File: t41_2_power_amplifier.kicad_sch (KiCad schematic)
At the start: 44 parts, among them J1 5-1814832-1, J2 5-1814832-1, J3 B2B-XH-A_LF__SN_, J5 Screw_Terminal_01x02, Q1 Q_NMOS_GSD, Q3 Q_NMOS_GSD, T1 Transformer_1P_SS, T2 Transformer_1P_1S, U1 MCP1802x-xx02xOT

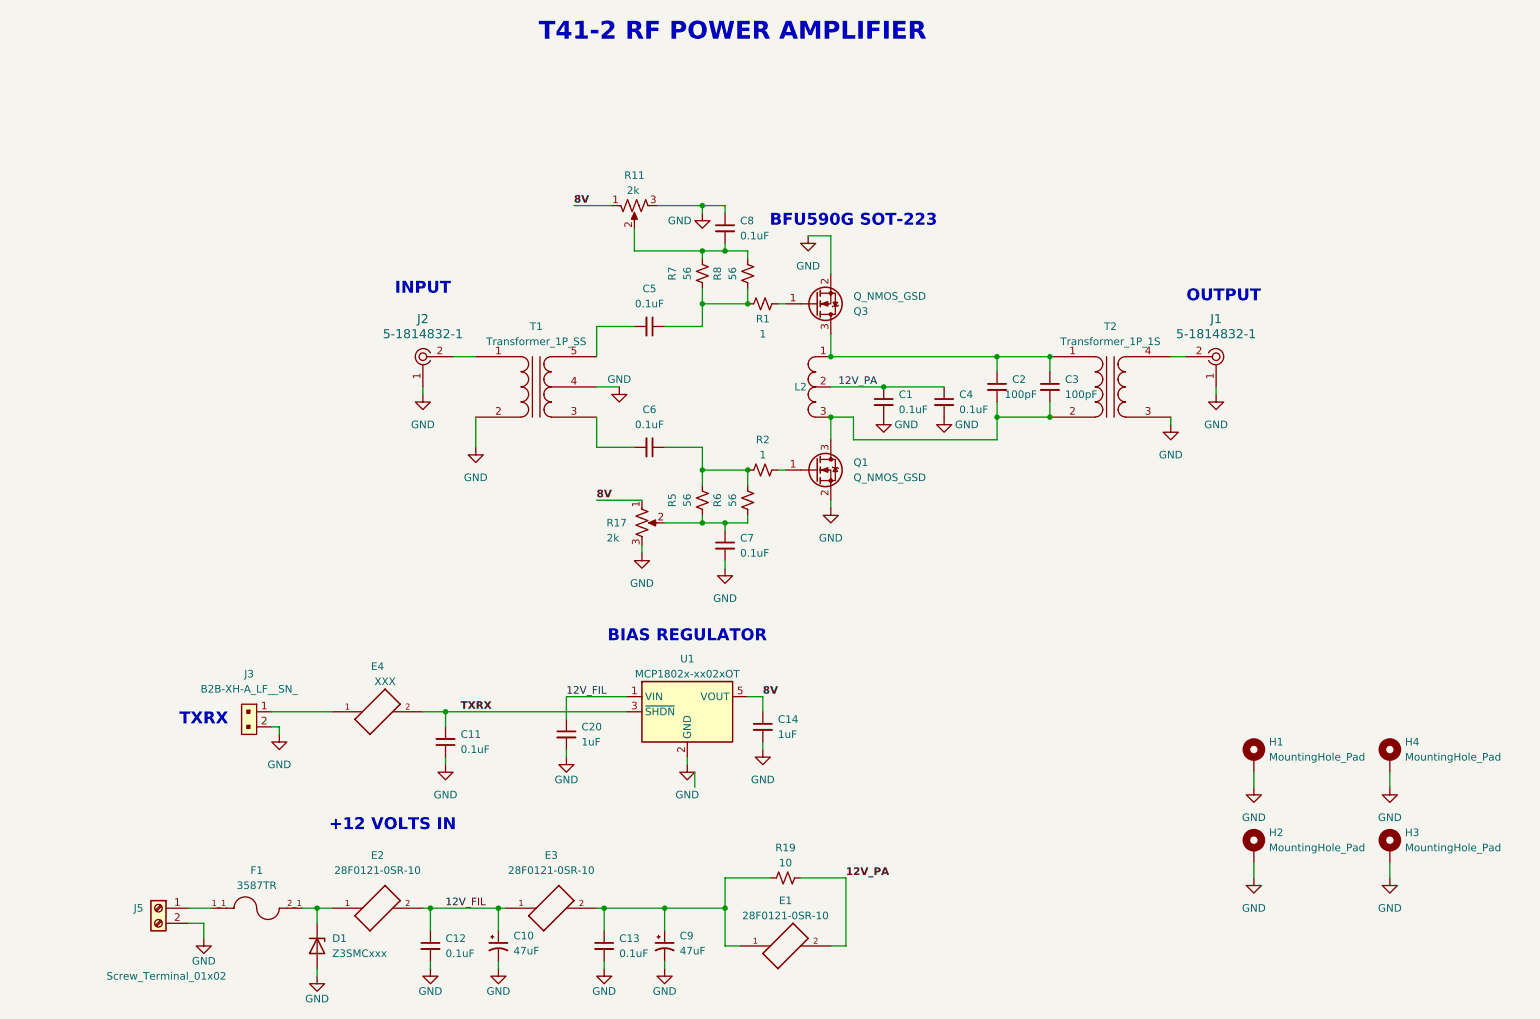
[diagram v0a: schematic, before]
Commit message: Larger output balun design to fab.
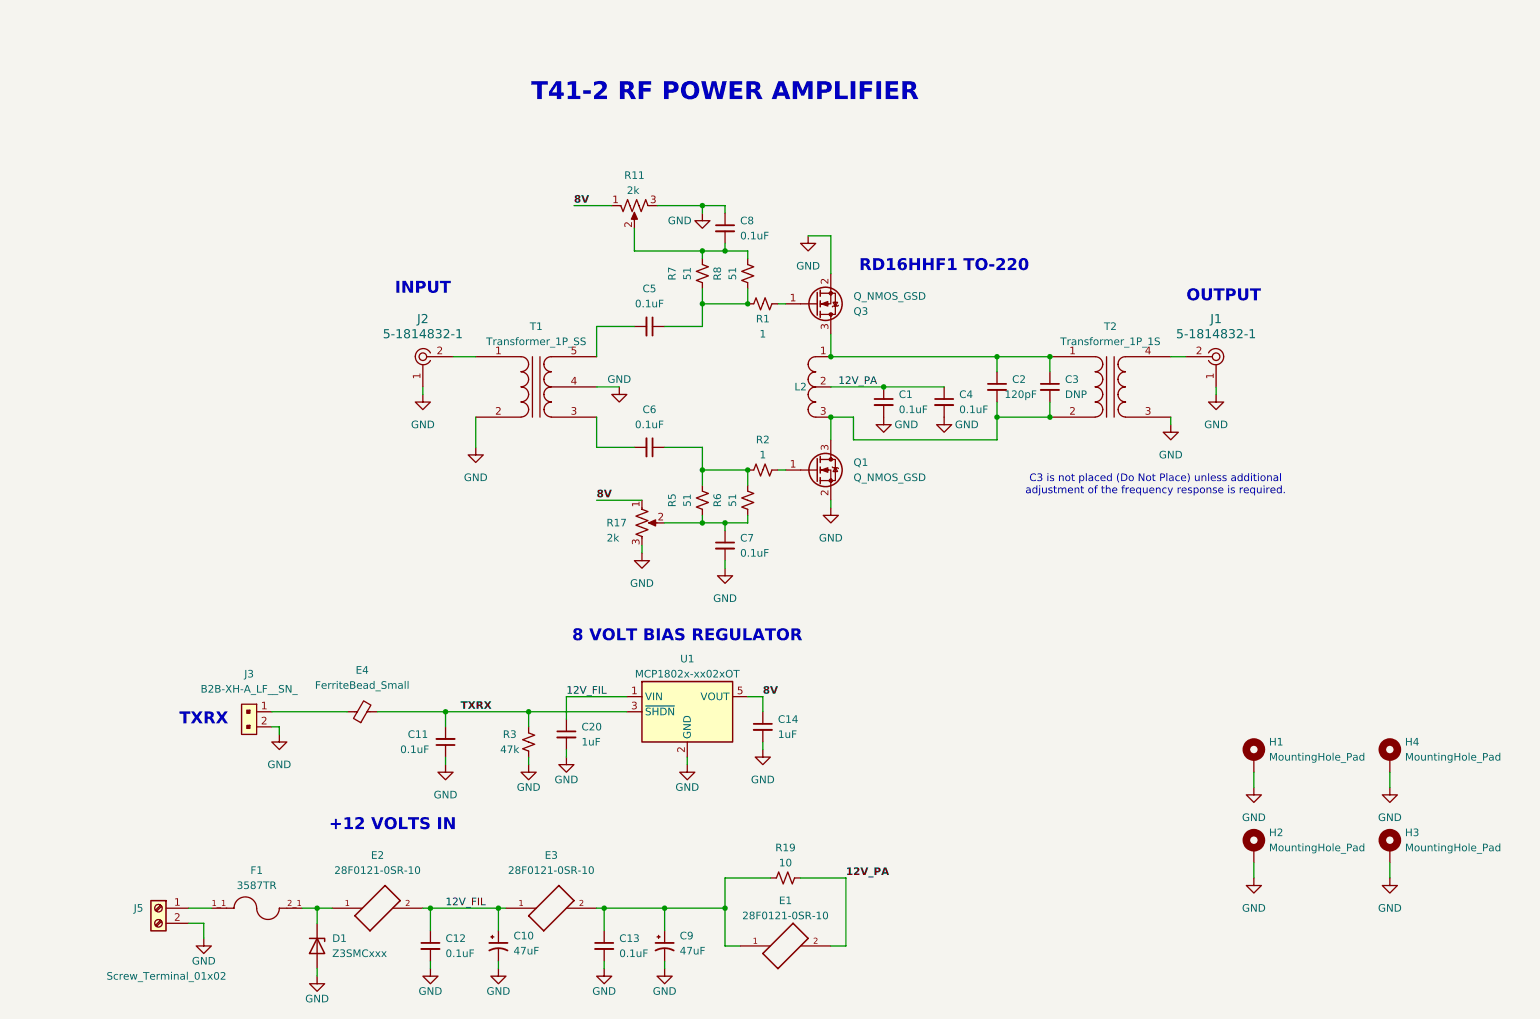
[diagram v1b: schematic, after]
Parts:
- removed E4: XXX, Inductor_SMD:L_1206_3216Metric, symbol 28F0121-0SR-10:28F0121-0SR-10
- added E4: FerriteBead_Small, Inductor_SMD:L_1206_3216Metric, symbol Device:FerriteBead_Small
- added R3: 47k, Resistor_SMD:R_1206_3216Metric, symbol Device:R_Small_US
- C2: value 100pF -> 120pF
- C3: value 100pF -> DNP
- R5, R6, R7, R8: value 56 -> 51
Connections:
- net GND: now also R3.1
- net TXRX: now also E4.2, R3.2
- net at J3.1: now also E4.1
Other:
- note added: "8 VOLT BIAS REGULATOR"
- note added: "C3 is not placed (Do Not Place) unless additional adjustment of the frequency response is required."
- note added: "RD16HHF1 TO-220"
- note removed: "BFU590G SOT-223"
- note removed: "BIAS REGULATOR"

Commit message: T41-2 Power Amplifier S to fab.
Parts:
- T2: footprint Binocular_Core:BN-43-7051 -> Binocular_Core:BN-43-3312
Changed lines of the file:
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@@
 			)
 		)
-		(property "Footprint" "Binocular_Core:BN-43-7051"
+		(property "Footprint" "Binocular_Core:BN-43-3312"
 			(at 193.04 78.74 0)
 			(effects

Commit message: Added zip files.
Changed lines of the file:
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@@
 (kicad_sch
-	(version 20231120)
+	(version 20250114)
 	(generator "eeschema")
-	(generator_version "8.0")
+	(generator_version "9.0")
 	(paper "USLetter")
 	(title_block
@@
 		(rev "1.3")
 	)
+	(text "OUTPUT"
+		(exclude_from_sim no)
+		(at 212.09 63.5 0)
+		(effects
+			(font
+				(size 2 2)
+				(thickness 0.4)
+				(bold yes)
+			)
+		)
+	)
+	(text "RD16HHF1 TO-220"
+		(exclude_from_sim no)
+		(at 165.1 58.42 0)
+		(effects
+			(font
+				(size 2 2)
+				(thickness 0.4)
+				(bold yes)
+			)
+		)
+	)
+	(text "+12 VOLTS IN"
+		(exclude_from_sim no)
+		(at 72.39 152.4 0)
+		(effects
+			(font
+				(size 2 2)
+				(thickness 0.4)
+				(bold yes)
+			)
+		)
+	)
+	(text "TXRX"
+		(exclude_from_sim no)
+		(at 40.64 134.62 0)
+		(effects
+			(font
+				(size 2 2)
+				(thickness 0.4)
+				(bold yes)
+			)
+		)
+	)
+	(text "T41-2 RF POWER AMPLIFIER"
+		(exclude_from_sim no)
+		(at 128.27 29.21 0)
+		(effects
+			(font
+				(size 3 3)
+				(thickness 0.6)
+				(bold yes)
+			)
+		)
+	)
+	(text "INPUT"
+		(exclude_from_sim no)
+		(at 77.47 62.23 0)
+		(effects
+			(font
+				(size 2 2)
+				(thickness 0.4)
+				(bold yes)
+			)
+		)
+	)
+	(text "C3 is not placed (Do Not Place) unless additional\nadjustment of the frequency response is required."
+		(exclude_from_sim no)
+		(at 200.66 95.25 0)
+		(effects
+			(font
+				(size 1.27 1.27)
+			)
+		)
+	)
+	(text "8 VOLT BIAS REGULATOR"
+		(exclude_from_sim no)
+		(at 121.92 120.65 0)
+		(effects
+			(font
+				(size 2 2)
+				(thickness 0.4)
+				(bold yes)
+			)
+		)
+	)
 	(junction
 		(at 78.74 166.37)
@@
 		)
 	)
-	(text "OUTPUT"
-		(exclude_from_sim no)
-		(at 212.09 63.5 0)
-		(effects
-			(font
-				(size 2 2)
-				(thickness 0.4)
-				(bold yes)
-			)
-		)
-	)
-	(text "RD16HHF1 TO-220"
-		(exclude_from_sim no)
-		(at 165.1 58.42 0)
-		(effects
-			(font
-				(size 2 2)
-				(thickness 0.4)
-				(bold yes)
-			)
-		)
-	)
-	(text "+12 VOLTS IN"
-		(exclude_from_sim no)
-		(at 72.39 152.4 0)
-		(effects
-			(font
-				(size 2 2)
-				(thickness 0.4)
-				(bold yes)
-			)
-		)
-	)
-	(text "TXRX"
-		(exclude_from_sim no)
-		(at 40.64 134.62 0)
-		(effects
-			(font
-				(size 2 2)
-				(thickness 0.4)
-				(bold yes)
-			)
-		)
-	)
-	(text "T41-2 RF POWER AMPLIFIER"
-		(exclude_from_sim no)
-		(at 128.27 29.21 0)
-		(effects
-			(font
-				(size 3 3)
-				(thickness 0.6)
-				(bold yes)
-			)
-		)
-	)
-	(text "INPUT"
-		(exclude_from_sim no)
-		(at 77.47 62.23 0)
-		(effects
-			(font
-				(size 2 2)
-				(thickness 0.4)
-				(bold yes)
-			)
-		)
-	)
-	(text "C3 is not placed (Do Not Place) unless additional\nadjustment of the frequency response is required."
-		(exclude_from_sim no)
-		(at 200.66 95.25 0)
-		(effects
-			(font
-				(size 1.27 1.27)
-			)
-		)
-	)
-	(text "8 VOLT BIAS REGULATOR"
-		(exclude_from_sim no)
-		(at 121.92 120.65 0)
-		(effects
-			(font
-				(size 2 2)
-				(thickness 0.4)
-				(bold yes)
-			)
-		)
-	)
 	(label "8V"
 		(at 106.68 97.79 0)
@@
 		)
 	)
+	(embedded_fonts no)
 )

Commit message: Released to fab.
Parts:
- removed C2: 120pF, Capacitor_SMD:C_1206_3216Metric, symbol Device:C_Small
- removed C3: DNP, Capacitor_SMD:C_1206_3216Metric, symbol Device:C_Small
- added C15, C16: 0.1uF, Capacitor_SMD:C_1206_3216Metric, symbol 28F0121-0SR-10:C_Small
- added T3: Transformer_1P_1S, Binocular_Core:BN-43-202, symbol 28F0121-0SR-10:Transformer_1P_1S
- C1, C11, C12, C13, C14, C20, C4, C5, C6, C7, C8: symbol Device:C_Small -> 28F0121-0SR-10:C_Small
- C10, C9: symbol Device:C_Polarized_Small_US -> 28F0121-0SR-10:C_Polarized_Small_US
- D1: symbol Diode:Z3SMCxxx -> 28F0121-0SR-10:Z3SMCxxx
- E4: symbol Device:FerriteBead_Small -> 28F0121-0SR-10:FerriteBead_Small
- F1: symbol Auto_Fuse_Holder:3587TR -> 28F0121-0SR-10:3587TR
- H1, H2, H3, H4: symbol Mechanical:MountingHole_Pad -> 28F0121-0SR-10:MountingHole_Pad
- J1, J2: symbol dk_Coaxial-Connectors-RF:5-1814832-1 -> 28F0121-0SR-10:5-1814832-1
- J3: symbol dk_Rectangular-Connectors-Headers-Male-Pins:B2B-XH-A_LF__SN_ -> 28F0121-0SR-10:B2B-XH-A_LF__SN_
- J5: symbol Connector:Screw_Terminal_01x02 -> 28F0121-0SR-10:Screw_Terminal_01x02
- L2: symbol InductorTapped:InductorTapped -> 28F0121-0SR-10:InductorTapped
- Q1, Q3: symbol Device:Q_NMOS_GSD -> 28F0121-0SR-10:Q_NMOS_GSD
- R1, R19, R2, R3, R5, R6, R7, R8: symbol Device:R_Small_US -> 28F0121-0SR-10:R_Small_US
- R11, R17: symbol Device:R_Potentiometer_US -> 28F0121-0SR-10:R_Potentiometer_US
- T1: symbol Device:Transformer_1P_SS -> 28F0121-0SR-10:Transformer_1P_SS
- T2: footprint Binocular_Core:BN-43-3312 -> Binocular_Core:BN-43-202; symbol Device:Transformer_1P_1S -> 28F0121-0SR-10:Transformer_1P_1S
- U1: symbol Regulator_Linear:MCP1802x-xx02xOT -> 28F0121-0SR-10:MCP1802x-xx02xOT
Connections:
- net 12V_PA: now also T2.2 (AB), C15.1, C16.1, T3.1 (AA)
- net GND: now also C15.2, C16.2, T3.3 (SA)
- net at L2.3, Q1.3 (D): now also T3.2 (AB); no longer T2.2 (AB)
- net at J1.2, T2.4 (SB): now also T3.4 (SB)
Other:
- moved on the sheet: J1, T2

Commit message: Added notes to schematic.
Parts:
- added R4: 0 OHM, Resistor_SMD:R_1206_3216Metric, symbol 28F0121-0SR-10:R_Small_US
- Q1, Q3: footprint TO-220_RF:TO-220_RF_Flat -> TO-220_RF:TO-220_RF_Flat_Through_Hole
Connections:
- net 12V_FIL: now also R4.1; no longer C20.1, U1.1 (VIN)
- net 12V_PA: no longer C15.1, C16.1, T2.2 (AB), T3.1 (AA)
- net GND: now also T2.2 (AB), T3.1 (AA); no longer C15.2, C16.2
- net at L2.3, Q1.3 (D): now also C16.1; no longer T3.2 (AB)
- net at L2.1, Q3.3 (D): now also C15.1; no longer T2.1 (AA)
- new net: C15.2, T2.1 (AA)
- new net: C20.1, R4.2, U1.1 (VIN)
- new net: C16.2, T3.2 (AB)
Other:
- note added: "1 TURN TWISTED PAIR #24"
- note added: "2 TURNS #24"
- note added: "BN-43-202"
- note added: "BN-43-302"
- note added: "T2 and T3 PRIMARY 1 TURN SECONDARY 4 TURNS BN-43-202"
- moved on the sheet: C15, C16, J1, T2, T3

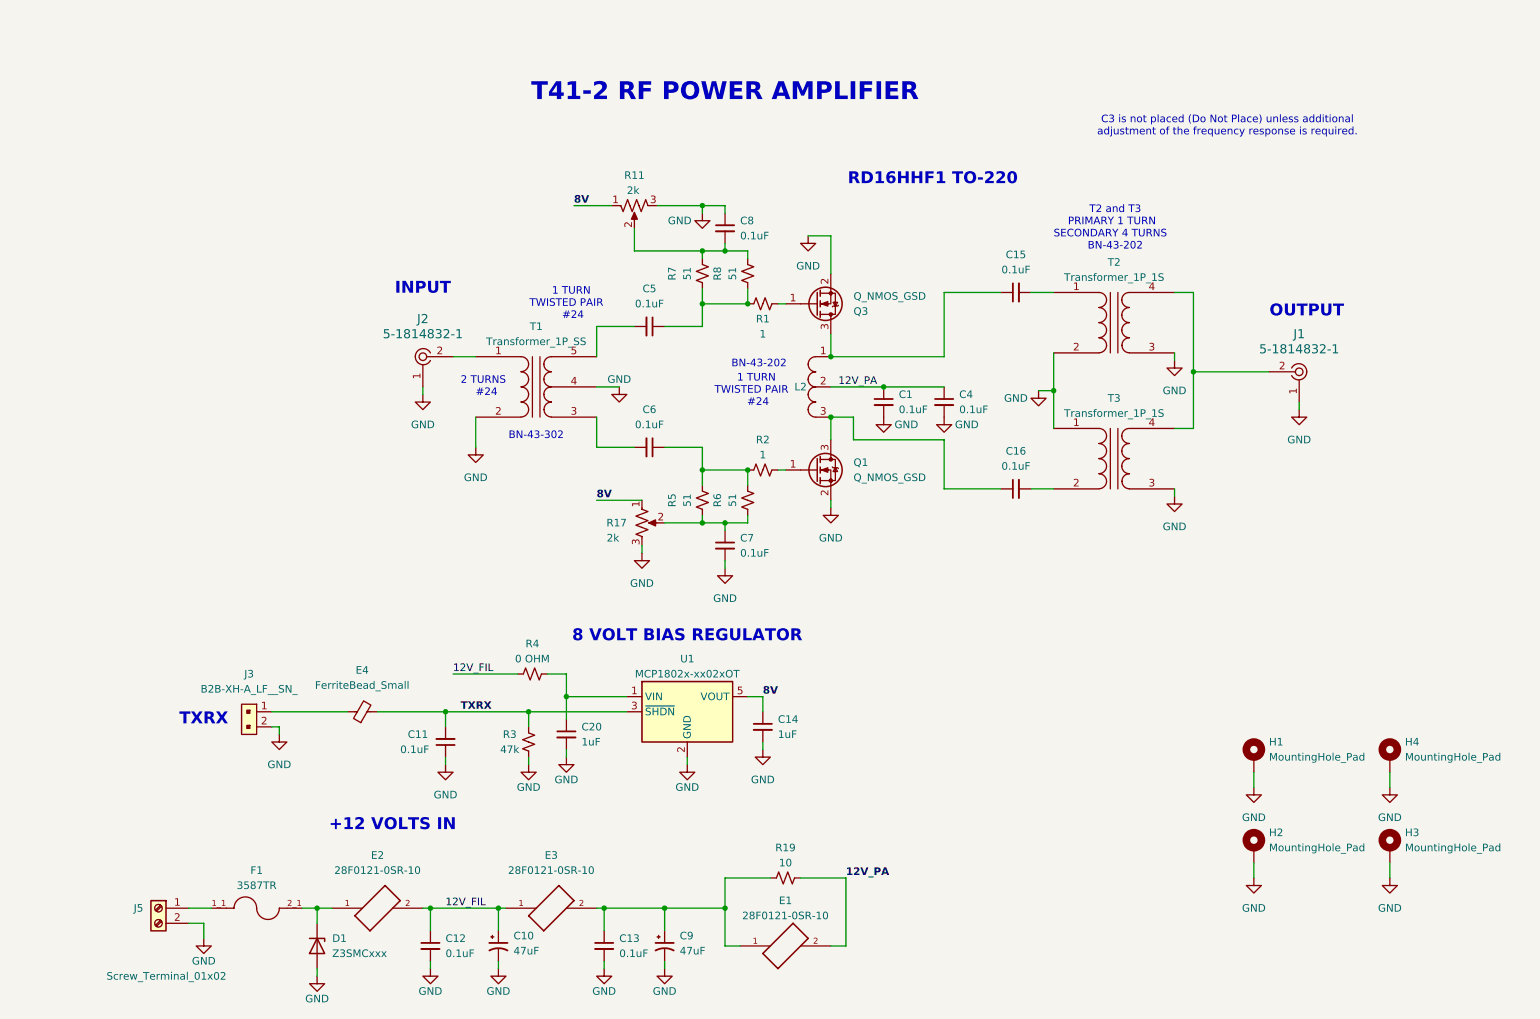
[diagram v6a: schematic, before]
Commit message: Added new bypass capacitors.  Added thermostat circuit.
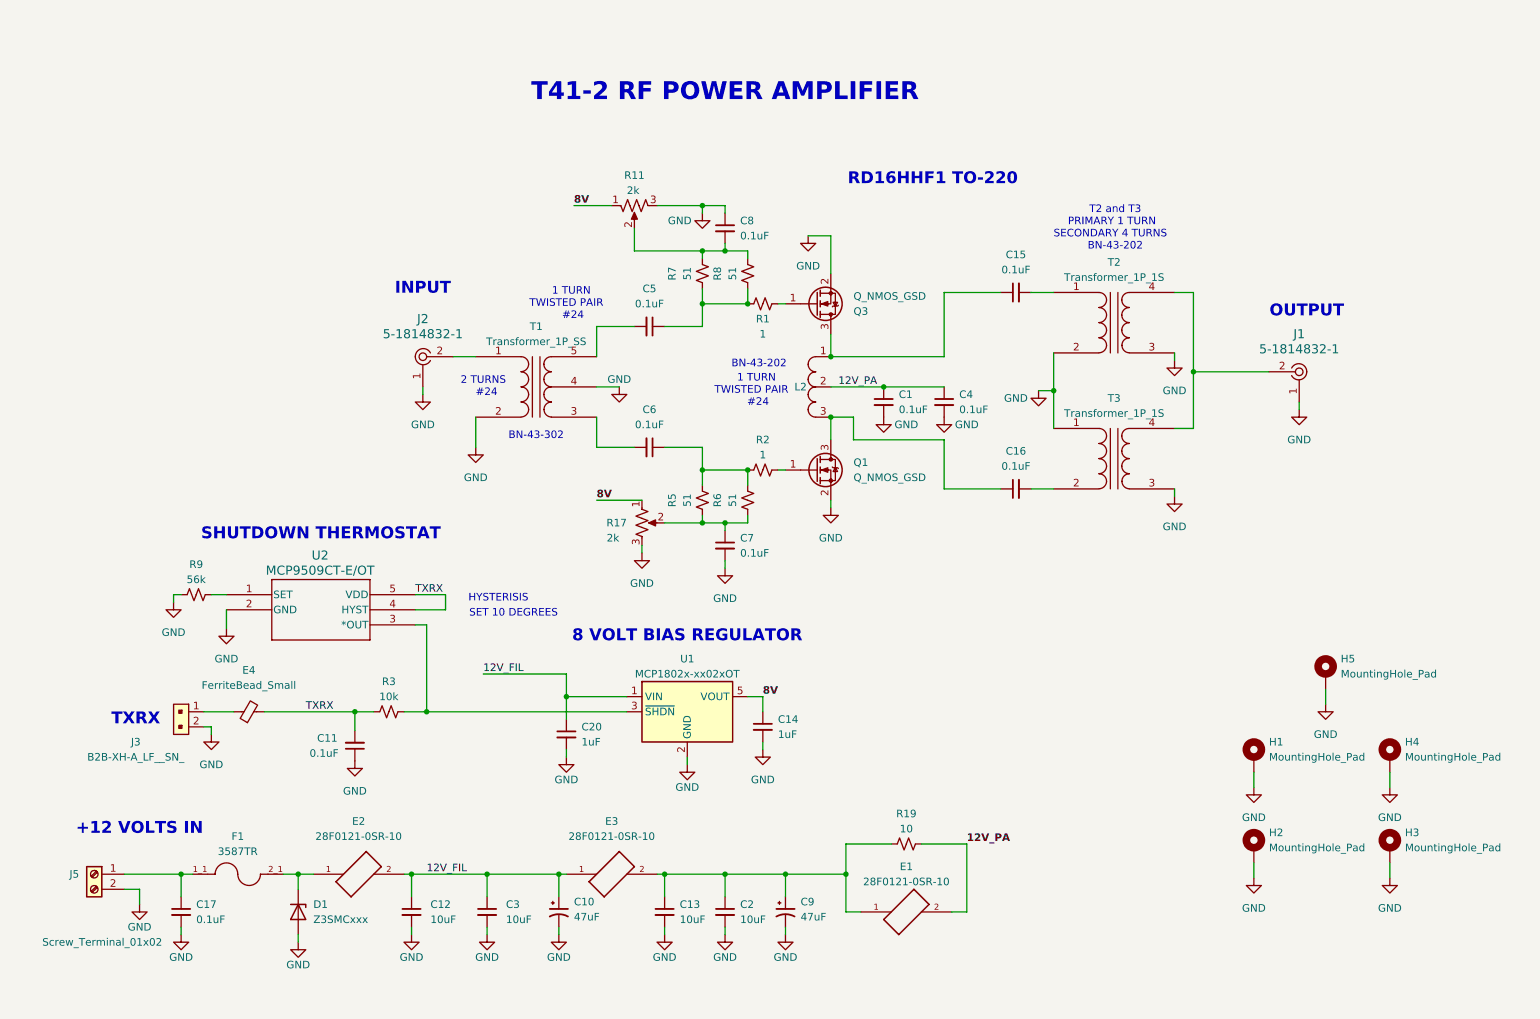
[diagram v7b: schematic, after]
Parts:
- removed R4: 0 OHM, Resistor_SMD:R_1206_3216Metric, symbol 28F0121-0SR-10:R_Small_US
- added C17: 0.1uF, Capacitor_SMD:C_1206_3216Metric, symbol 28F0121-0SR-10:C_Small
- added C2, C3: 10uF, Capacitor_SMD:C_1206_3216Metric, symbol 28F0121-0SR-10:C_Small
- added H5: MountingHole_Pad, MountingHole:MountingHole_4.3mm_M4_DIN965_Pad, symbol 28F0121-0SR-10:MountingHole_Pad
- added R9: 56k, Resistor_SMD:R_1206_3216Metric, symbol 28F0121-0SR-10:R_Small_US
- added U2: MCP9509CT-E/OT, SOT-23-5_MC_MCH, symbol MCP9509:MCP9509CT-E_OT
- C12, C13: value 0.1uF -> 10uF
- R3: value 47k -> 10k
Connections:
- net 12V_FIL: now also C20.1, U1.1 (VIN), C3.1
- net GND: now also C17.2, C2.2, C3.2, H5.1, R9.1, U2.2 (GND); no longer R3.1
- net TXRX: now also R3.1, U2.4 (HYST), U2.5 (VDD); no longer R3.2, U1.3 (~{SHDN})
- net at F1.1_1, J5.1 (Pin_1): now also C17.1
- net at C13.1, C9.1, E1.1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: now also C2.1
- new net: R3.2, U1.3 (~{SHDN}), U2.3 (*OUT)
- new net: R9.2, U2.1 (SET)
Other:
- note added: "HYSTERISIS"
- note added: "SET 10 DEGREES"
- note added: "SHUTDOWN THERMOSTAT"
- note removed: "C3 is not placed (Do Not Place) unless additional adjustment of the frequency response is required."
- moved on the sheet: C10, C11, C12, C13, C9, D1, E1, E2, E3, E4, F1, J3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

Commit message: Work in progress.
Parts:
- C11: value 0.1uF -> 0.01uF
- C14: value 1uF -> 0.1uF
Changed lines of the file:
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@@
 			)
 		)
-		(property "Value" "1uF"
+		(property "Value" "0.1uF"
 			(at 137.16 137.1662 0)
 			(effects
@@
 		(dnp no)
 		(property "Reference" "C11"
-			(at 59.69 137.795 0)
+			(at 58.42 139.065 0)
 			(effects
 				(font
@@
 			)
 		)
-		(property "Value" "0.1uF"
-			(at 58.42 140.335 0)
-			(effects
-				(font
+		(property "Value" "0.01uF"
+			(at 57.15 140.97 0)
+			(effects
+				(font
